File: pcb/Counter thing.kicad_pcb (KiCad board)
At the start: 2 copper layers, 61 x 34 mm, 13 parts, among them J1 FTSH-105-01-L-DV-007-K, SW1 B3FS-1015, U1 STM32L010K4T6

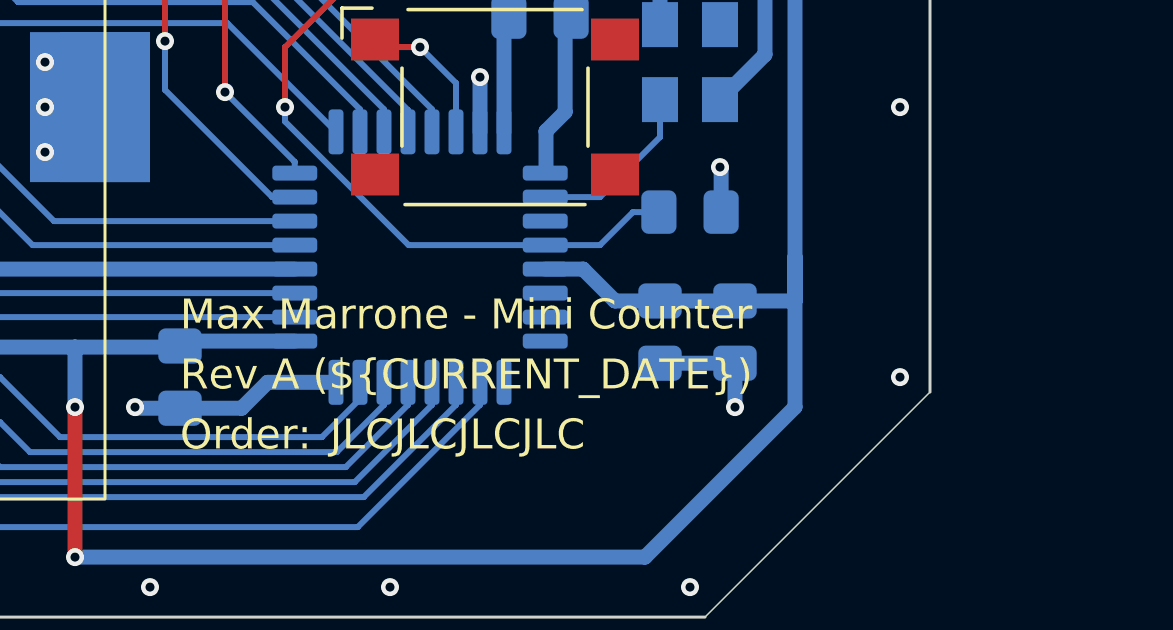
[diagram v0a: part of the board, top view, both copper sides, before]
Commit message: Update KiCad page titles.
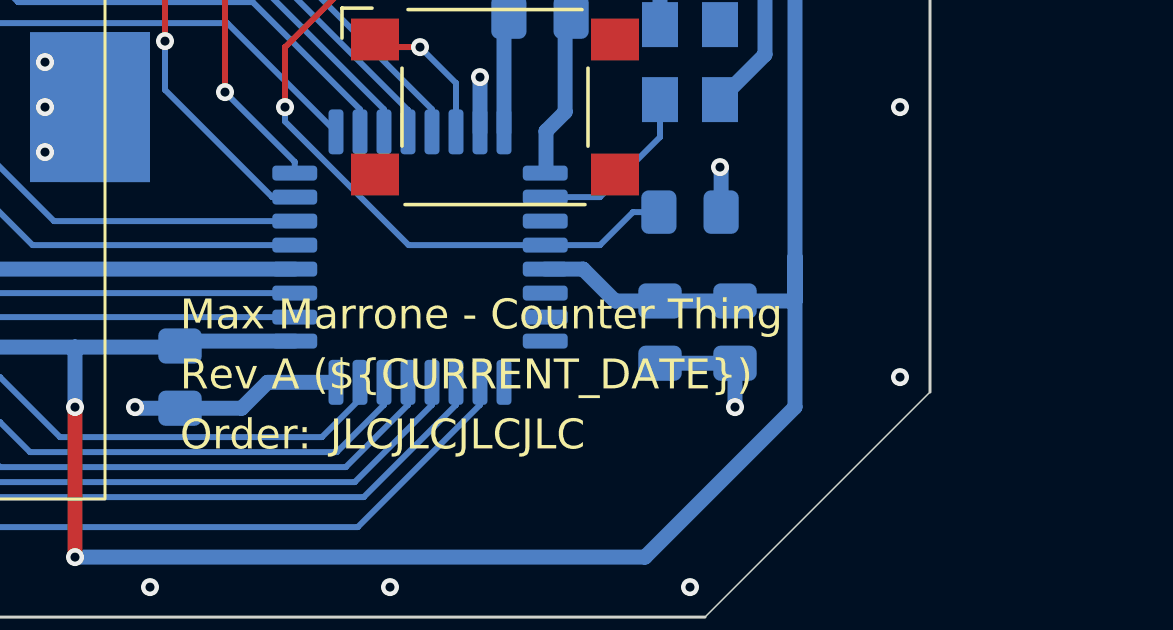
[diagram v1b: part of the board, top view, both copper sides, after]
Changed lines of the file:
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@@
 	(paper "A4")
 	(title_block
-		(title "Mini Counter")
+		(title "Counter Thing")
 		(rev "A")
 		(company "Max Marrone")
